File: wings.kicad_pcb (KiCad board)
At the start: 2 copper layers, 147.9 x 119.9 mm, 66 parts

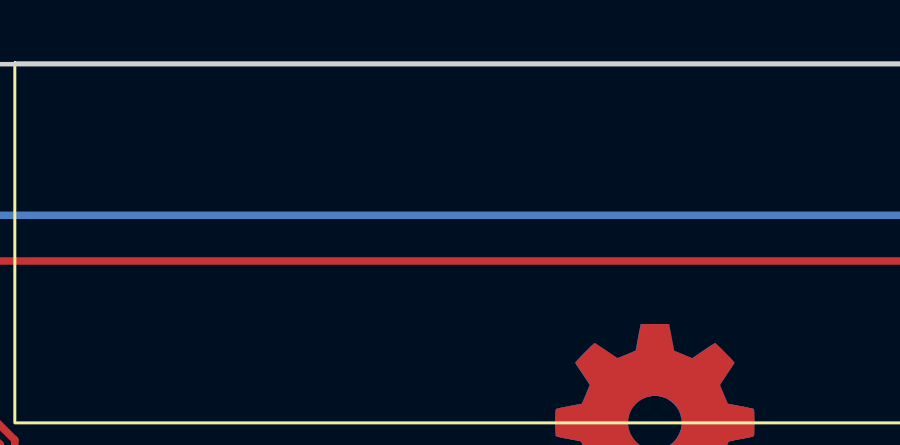
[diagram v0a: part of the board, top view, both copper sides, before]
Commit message: add version markings and new production files
this is the version send to production!
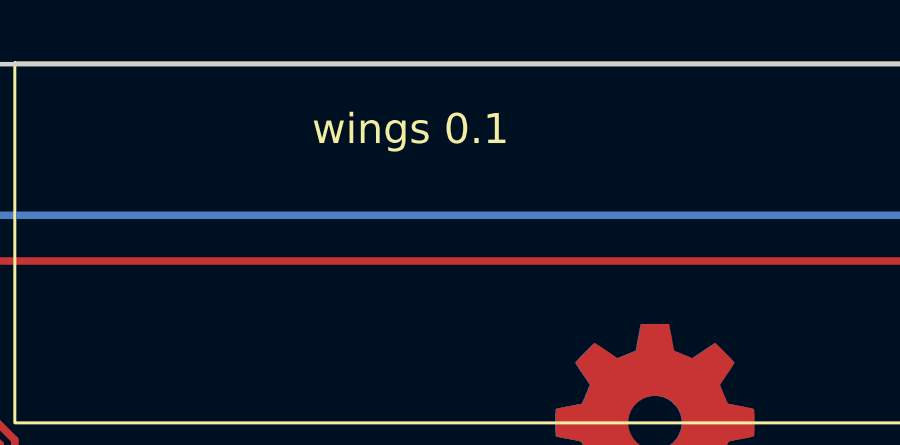
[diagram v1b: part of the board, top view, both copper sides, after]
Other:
- board text added: "wings 0.1"
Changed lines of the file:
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@@
+		)
+	)
+	(gr_text "wings 0.1"
+		(at 113.03 31.75 0)
+		(layer "B.SilkS")
+		(effects
+			(font
+				(size 1 1)
+				(thickness 0.15)
+			)
+			(justify left bottom mirror)
+		)
+	)
+	(gr_text "wings 0.1"
+		(at 105.41 31.75 0)
+		(layer "F.SilkS")
+		(effects
+			(font
+				(size 1 1)
+				(thickness 0.15)
+			)
+			(justify left bottom)
 		)
 	)
